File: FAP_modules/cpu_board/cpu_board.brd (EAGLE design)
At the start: 100 x 60 mm, 34 parts, among them IC2 74HC245DW, IC3 74HC245DW, IC4 74HC04D, IC7 74HC245DW, IC8 74HC245DW, IC9 74HC245DW

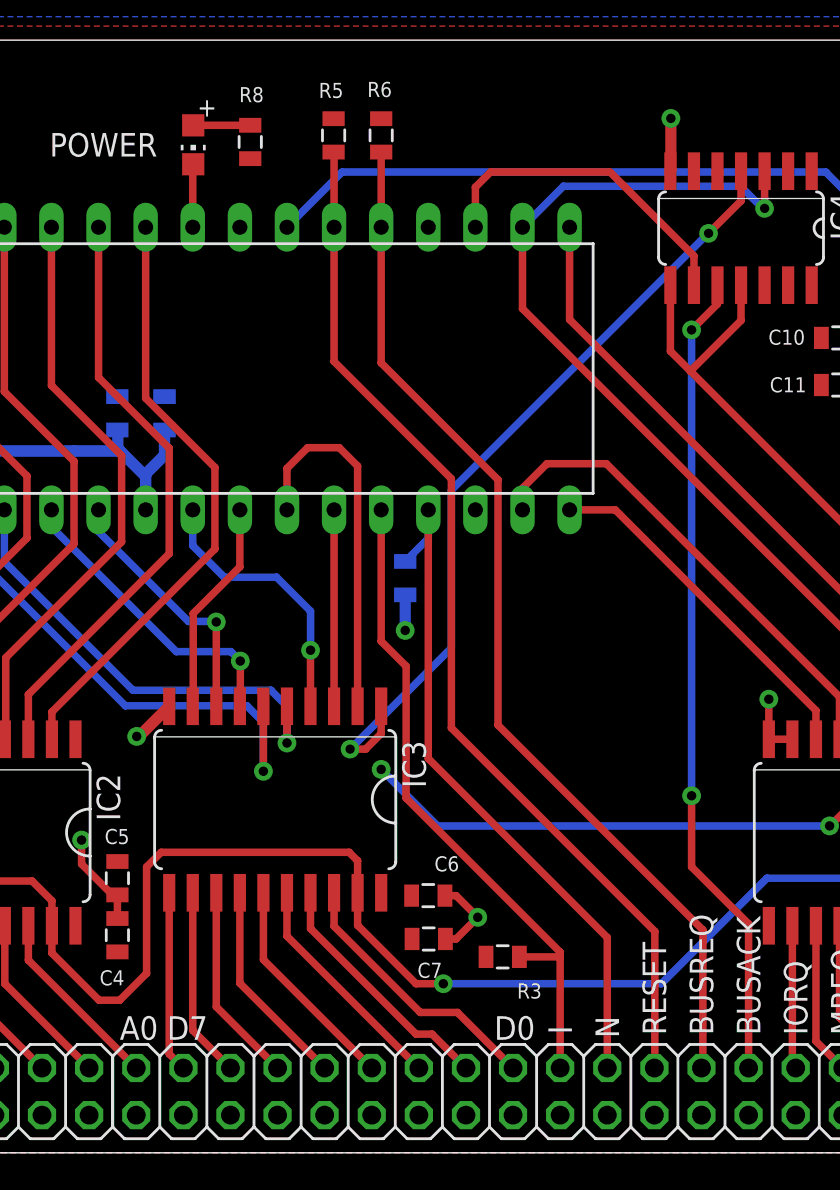
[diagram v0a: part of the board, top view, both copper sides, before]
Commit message: added interrupt chaining and WAIT
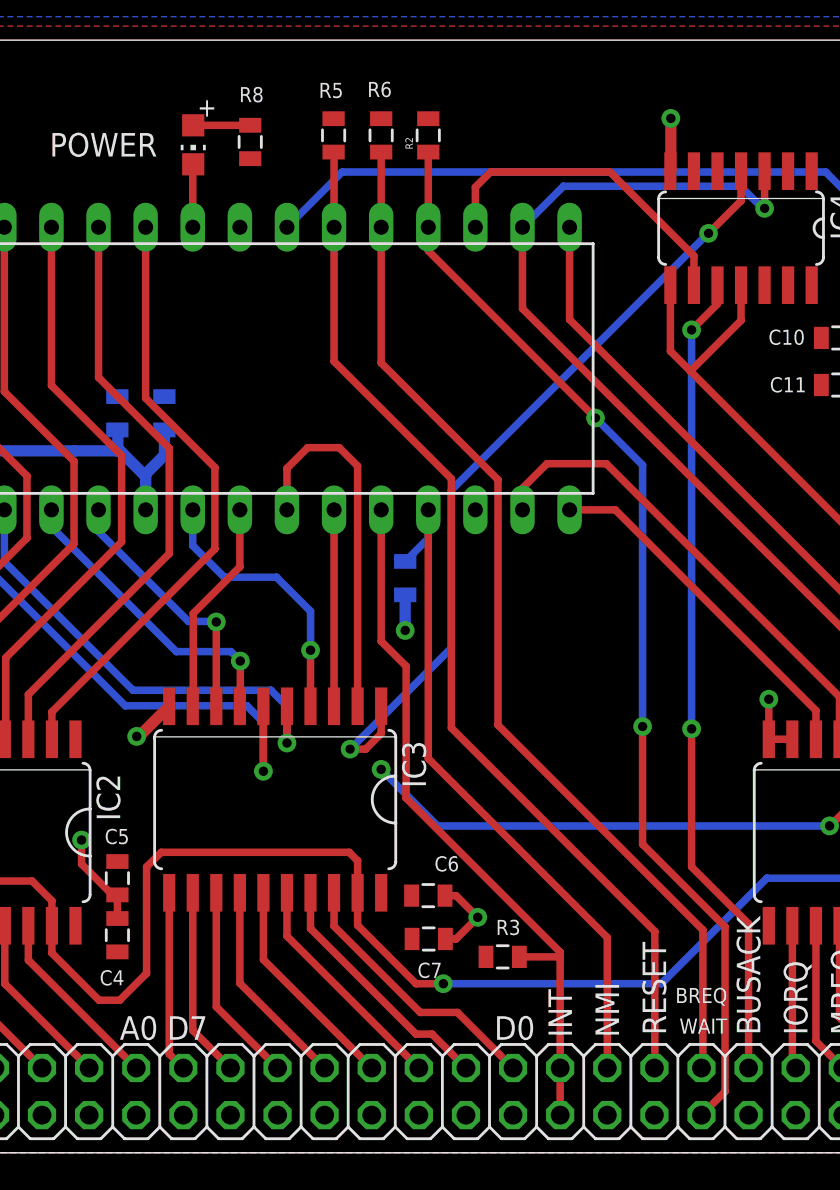
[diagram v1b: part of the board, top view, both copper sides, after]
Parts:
- added R2: (no value), SparkFun-Resistors:0805
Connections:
- new net N$32: IC1.24, R2.1, U$1.WAIT
- net +3V3: now also R2.2; no longer IC1.24
- net GND: no longer U$1.GND@29, U$1.GND@32
- net N$35: now also U$1.INTI, U$1.INTO; no longer U$1.INT
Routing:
- net N$32: track 0.00 -> 59.1 mm, vias 0 -> 2
- net N$35: track 36.3 -> 38.9 mm
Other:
- board text added: "BREQ"
- board text added: "INT"
- board text added: "NMI"
- board text added: "WAIT"
- board text removed: "BUSREQ"
- board text removed: "I"
- board text removed: "N"
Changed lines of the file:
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@@
 <?xml version="1.0" encoding="utf-8"?>
 <!DOCTYPE eagle SYSTEM "eagle.dtd">
-<eagle version="7.7.0">
+<eagle version="7.6.0">
 <drawing>
 <settings>
@@
 <setting verticaltext="up"/>
 </settings>
-<grid distance="20" unitdist="mil" unit="mil" style="lines" multiple="1" display="no" altdistance="0.5" altunitdist="mil" altunit="mil"/>
+<grid distance="5" unitdist="mil" unit="mil" style="lines" multiple="1" display="no" altdistance="0.5" altunitdist="mil" altunit="mil"/>
 <layers>
 <layer number="1" name="Top" color="4" fill="1" visible="yes" active="yes"/>
@@
 <text x="22.606" y="6.096" size="1.27" layer="25">A8</text>
 <text x="4.064" y="6.096" size="1.27" layer="25">A15</text>
-<text x="73.533" y="6.858" size="1.27" layer="25" rot="R270">I</text>
-<text x="76.073" y="7.366" size="1.27" layer="25" rot="R270">N</text>
+<text x="74.803" y="6.223" size="1.27" layer="25" rot="R90">INT</text>
+<text x="77.343" y="6.223" size="1.27" layer="25" rot="R90">NMI</text>
 <text x="79.883" y="6.35" size="1.27" layer="25" rot="R90">RESET</text>
-<text x="82.423" y="6.35" size="1.27" layer="25" rot="R90">BUSREQ</text>
+<text x="83.185" y="8.89" size="0.8128" layer="25" rot="R180">BREQ</text>
 <text x="84.963" y="6.35" size="1.27" layer="25" rot="R90">BUSACK</text>
 <text x="87.503" y="6.35" size="1.27" layer="25" rot="R90">IORQ</text>
@@
 dekuNukem 2016</text>
 <text x="46.6344" y="53.721" size="1.27" layer="25">POWER</text>
+<text x="83.185" y="7.239" size="0.8128" layer="25" rot="R180">WAIT</text>
 </plain>
 <attributes>
@@
 </element>
 <element name="R3" library="SparkFun-Resistors" package="0805" value="" x="71.0692" y="10.5664" smashed="yes" rot="R180">
-<attribute name="NAME" x="73.1774" y="9.1313" size="0.8128" layer="25" rot="R180"/>
+<attribute name="NAME" x="72.0344" y="12.5603" size="0.8128" layer="25" rot="R180"/>
 <attribute name="VALUE" x="72.0852" y="11.9634" size="0.4064" layer="27" rot="R180"/>
 </element>
@@
 </element>
 <element name="R1" library="SparkFun-Resistors" package="0805" value="" x="33.9598" y="15.875" rot="MR90"/>
+<element name="R2" library="SparkFun-Resistors" package="0805" value="" x="67.056" y="54.864" rot="R90"/>
 </elements>
 <signals>
@@
 <contactref element="R5" pad="2"/>
 <contactref element="R6" pad="2"/>
-<contactref element="IC1" pad="24"/>
 <contactref element="IC3" pad="20"/>
 <via x="65.8114" y="28.1686" extent="1-16" drill="0.508"/>
@@
 <wire x1="32.3723" y1="16.7767" x2="33.9581" y2="16.7767" width="0.4064" layer="16"/>
 <wire x1="33.9581" y1="16.7767" x2="33.9598" y2="16.775" width="0.4064" layer="16"/>
+<contactref element="R2" pad="2"/>
 </signal>
 <signal name="+5V">
@@
 <wire x1="82.6516" y1="45.7708" x2="81.2546" y2="44.3738" width="0.4064" layer="1"/>
 <via x="81.2546" y="44.3738" extent="1-16" drill="0.508"/>
-<via x="81.2546" y="19.2532" extent="1-16" drill="0.508"/>
-<wire x1="81.2546" y1="19.2532" x2="81.2546" y2="15.4178" width="0.4064" layer="1"/>
+<via x="81.2546" y="22.86" extent="1-16" drill="0.508"/>
+<wire x1="81.2546" y1="22.86" x2="81.2546" y2="15.4178" width="0.4064" layer="1"/>
 <wire x1="81.2546" y1="15.4178" x2="84.328" y2="12.3444" width="0.4064" layer="1"/>
-<wire x1="81.2546" y1="44.3738" x2="81.2546" y2="19.2532" width="0.4064" layer="16"/>
+<wire x1="81.2546" y1="44.3738" x2="81.2546" y2="22.86" width="0.4064" layer="16"/>
 </signal>
 <signal name="N$26">
@@
 <contactref element="IC1" pad="16"/>
 <contactref element="R3" pad="1"/>
-<contactref element="U$1" pad="INT"/>
+<contactref element="U$1" pad="INTI"/>
 <wire x1="64.516" y1="34.671" x2="64.516" y2="27.5844" width="0.4064" layer="1"/>
 <wire x1="64.516" y1="27.5844" x2="65.8622" y2="26.2382" width="0.4064" layer="1"/>
@@
 <wire x1="65.8622" y1="19.1262" x2="74.168" y2="10.8204" width="0.4064" layer="1"/>
 <wire x1="74.168" y1="10.8204" x2="74.168" y2="10.6172" width="0.4064" layer="1"/>
-<wire x1="74.168" y1="10.6172" x2="74.168" y2="4.572" width="0.4064" layer="1"/>
-<wire x1="71.9692" y1="10.5664" x2="74.1172" y2="10.5664" width="0.4064" layer="1"/>
+<wire x1="71.9692" y1="10.5664" x2="74.041" y2="10.5664" width="0.4064" layer="1"/>
+<wire x1="74.041" y1="10.5664" x2="74.1172" y2="10.5664" width="0.4064" layer="1"/>
 <wire x1="74.1172" y1="10.5664" x2="74.168" y2="10.6172" width="0.4064" layer="1"/>
+<contactref element="U$1" pad="INTO"/>
+<wire x1="74.168" y1="4.572" x2="74.168" y2="10.4394" width="0.4064" layer="1"/>
+<wire x1="74.168" y1="10.4394" x2="74.041" y2="10.5664" width="0.4064" layer="1"/>
+<wire x1="74.168" y1="4.572" x2="74.168" y2="2.032" width="0.4064" layer="1"/>
 </signal>
 <signal name="N$39">
@@
 <contactref element="U$1" pad="GND@21"/>
 <contactref element="U$1" pad="GND@7"/>
-<contactref element="U$1" pad="GND@29"/>
 <contactref element="U$1" pad="GND@23"/>
 <contactref element="U$1" pad="GND@30"/>
@@
 <contactref element="U$1" pad="GND@15"/>
 <contactref element="U$1" pad="GND@25"/>
-<contactref element="U$1" pad="GND@32"/>
 <contactref element="U$1" pad="GND@18"/>
 <contactref element="U$1" pad="GND@28"/>
@@
 <wire x1="83.9216" y1="51.3334" x2="83.9216" y2="52.9336" width="0.4064" layer="1"/>
 </signal>
+<signal name="N$32">
+<contactref element="U$1" pad="WAIT"/>
+<contactref element="IC1" pad="24"/>
+<contactref element="R2" pad="1"/>
+<wire x1="67.056" y1="53.964" x2="67.056" y2="49.911" width="0.4064" layer="1"/>
+<wire x1="67.056" y1="49.911" x2="67.056" y2="48.641" width="0.4064" layer="1"/>
+<wire x1="67.056" y1="48.641" x2="76.073" y2="39.624" width="0.4064" layer="1"/>
+<via x="76.073" y="39.624" extent="1-16" drill="0.5"/>
+<wire x1="76.073" y1="39.624" x2="78.613" y2="37.084" width="0.4064" layer="16"/>
+<wire x1="78.613" y1="37.084" x2="78.613" y2="22.987" width="0.4064" layer="16"/>
+<via x="78.613" y="22.987" extent="1-16" drill="0.5"/>
+<wire x1="78.613" y1="22.987" x2="78.613" y2="16.637" width="0.4064" layer="1"/>
+<wire x1="78.613" y1="16.637" x2="83.058" y2="12.192" width="0.4064" layer="1"/>
+<wire x1="83.058" y1="12.192" x2="83.058" y2="3.302" width="0.4064" layer="1"/>
+<wire x1="83.058" y1="3.302" x2="81.788" y2="2.032" width="0.4064" layer="1"/>
+</signal>
 </signals>

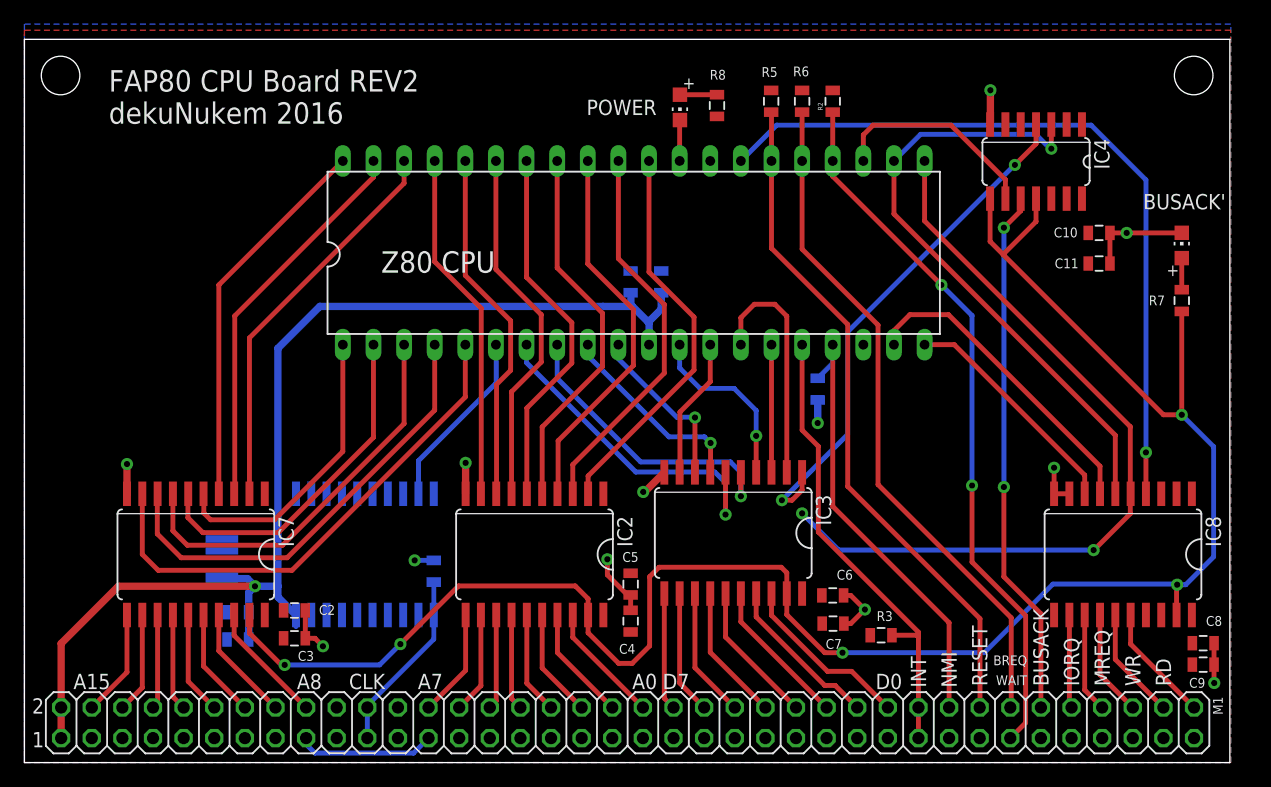
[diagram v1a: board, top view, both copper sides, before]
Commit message: new memory board
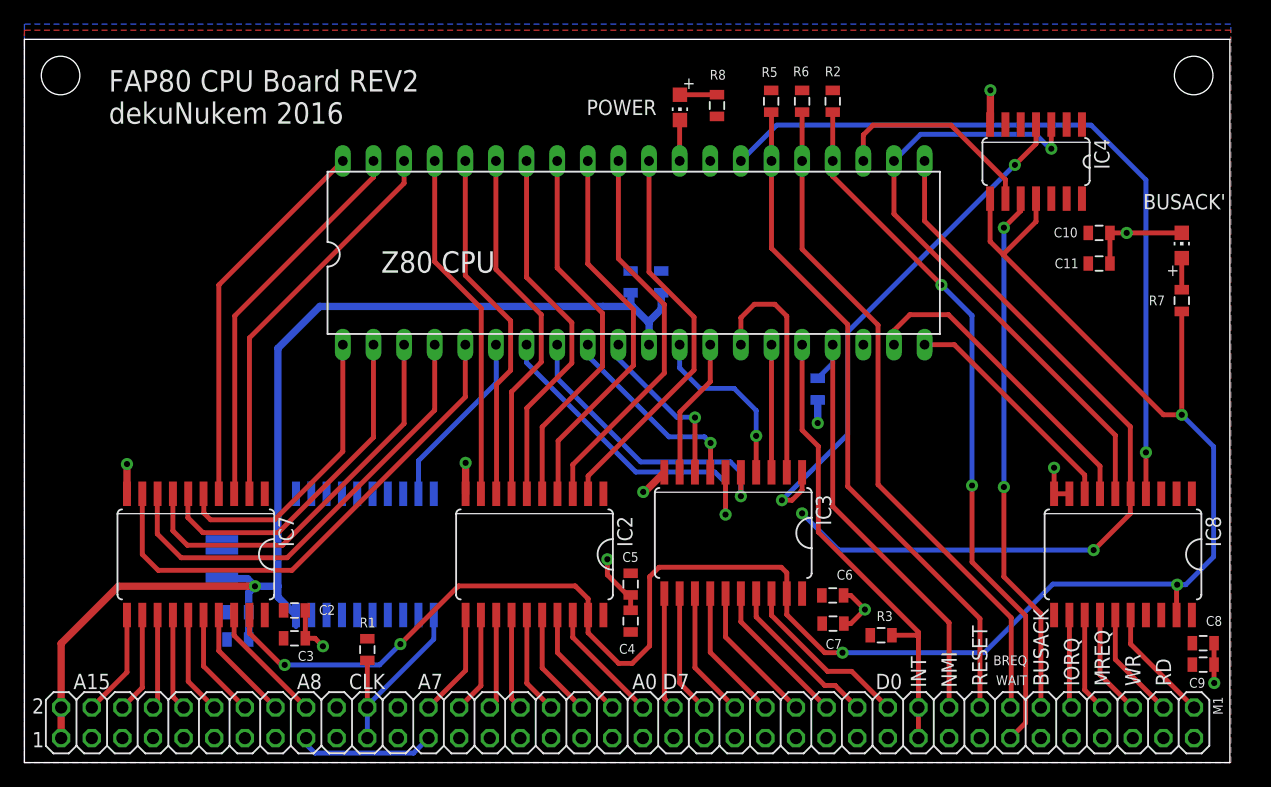
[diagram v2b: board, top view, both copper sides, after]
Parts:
- R1, R2, R3, R4, R5, R6: value (none) -> 4.7K
- R7, R8: value 50 -> 2K
- moved R1 8.52 mm to (28.4, 9.37), flipped to the top
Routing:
- net N$26: track 15.2 -> 16.9 mm
- net +3V3: track 3.51 -> 1.92 mm, vias 2 -> 1
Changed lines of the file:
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@@
 <?xml version="1.0" encoding="utf-8"?>
 <!DOCTYPE eagle SYSTEM "eagle.dtd">
-<eagle version="7.6.0">
+<eagle version="7.7.0">
 <drawing>
 <settings>
@@
 <setting verticaltext="up"/>
 </settings>
-<grid distance="5" unitdist="mil" unit="mil" style="lines" multiple="1" display="no" altdistance="0.5" altunitdist="mil" altunit="mil"/>
+<grid distance="1" unitdist="mil" unit="mil" style="lines" multiple="1" display="no" altdistance="0.5" altunitdist="mil" altunit="mil"/>
 <layers>
 <layer number="1" name="Top" color="4" fill="1" visible="yes" active="yes"/>
@@
 <attribute name="NAME" x="21.3868" y="20.447" size="1.27" layer="26" ratio="10" rot="MR270"/>
 </element>
-<element name="R3" library="SparkFun-Resistors" package="0805" value="" x="71.0692" y="10.5664" smashed="yes" rot="R180">
+<element name="R3" library="SparkFun-Resistors" package="0805" value="4.7K" x="71.0692" y="10.5664" smashed="yes" rot="R180">
 <attribute name="NAME" x="72.0344" y="12.5603" size="0.8128" layer="25" rot="R180"/>
 <attribute name="VALUE" x="72.0852" y="11.9634" size="0.4064" layer="27" rot="R180"/>
 </element>
-<element name="R4" library="SparkFun-Resistors" package="0805" value="" x="65.8114" y="30.988" smashed="yes" rot="MR270">
+<element name="R4" library="SparkFun-Resistors" package="0805" value="4.7K" x="65.8114" y="30.988" smashed="yes" rot="MR270">
 <attribute name="NAME" x="64.5795" y="31.5976" size="0.8128" layer="26" rot="MR270"/>
 <attribute name="VALUE" x="67.2084" y="32.004" size="0.4064" layer="28" rot="MR270"/>
 </element>
-<element name="R5" library="SparkFun-Resistors" package="0805" value="" x="61.9506" y="54.864" smashed="yes" rot="R90">
+<element name="R5" library="SparkFun-Resistors" package="0805" value="4.7K" x="61.9506" y="54.864" smashed="yes" rot="R90">
 <attribute name="NAME" x="62.484" y="57.6961" size="0.8128" layer="25" rot="R180"/>
-<attribute name="VALUE" x="63.3476" y="53.848" size="0.4064" layer="27" rot="R90"/>
-</element>
-<element name="R6" library="SparkFun-Resistors" package="0805" value="" x="64.516" y="54.864" smashed="yes" rot="R90">
+</element>
+<element name="R6" library="SparkFun-Resistors" package="0805" value="4.7K" x="64.516" y="54.864" smashed="yes" rot="R90">
 <attribute name="NAME" x="65.1002" y="57.7469" size="0.8128" layer="25" rot="R180"/>
-<attribute name="VALUE" x="65.913" y="53.848" size="0.4064" layer="27" rot="R90"/>
 </element>
 <element name="C2" library="SparkFun-Capacitors" package="0805" value="10nF" x="22.4028" y="12.6238" smashed="yes">
@@
 <attribute name="VALUE" x="98.552" y="41.6306" size="1.27" layer="27" rot="R90"/>
 </element>
-<element name="R7" library="SparkFun-Passives" package="0805" value="50" x="96.012" y="38.3286" smashed="yes" rot="R90">
+<element name="R7" library="SparkFun-Passives" package="0805" value="2K" x="96.012" y="38.3286" smashed="yes" rot="R90">
 <attribute name="NAME" x="94.615" y="38.7477" size="0.8128" layer="25" rot="R180"/>
 </element>
@@
 <attribute name="VALUE" x="51.8414" y="55.626" size="1.27" layer="27" rot="R270"/>
 </element>
-<element name="R8" library="SparkFun-Passives" package="0805" value="50" x="57.4548" y="54.5084" smashed="yes" rot="R90">
+<element name="R8" library="SparkFun-Passives" package="0805" value="2K" x="57.4548" y="54.5084" smashed="yes" rot="R90">
 <attribute name="NAME" x="58.1914" y="57.4675" size="0.8128" layer="25" rot="R180"/>
 </element>
-<element name="R1" library="SparkFun-Resistors" package="0805" value="" x="33.9598" y="15.875" rot="MR90"/>
-<element name="R2" library="SparkFun-Resistors" package="0805" value="" x="67.056" y="54.864" rot="R90"/>
+<element name="R1" library="SparkFun-Resistors" package="0805" value="4.7K" x="28.448" y="9.3726" smashed="yes" rot="R90">
+<attribute name="NAME" x="29.1338" y="12.0269" size="0.8128" layer="25" rot="R180"/>
+</element>
+<element name="R2" library="SparkFun-Resistors" package="0805" value="4.7K" x="67.056" y="54.864" smashed="yes" rot="R90">
+<attribute name="NAME" x="67.7418" y="57.7469" size="0.8128" layer="25" rot="R180"/>
+</element>
 </elements>
 <signals>
@@
 <contactref element="IC8" pad="3"/>
 <contactref element="R1" pad="2"/>
-<via x="32.3723" y="16.7767" extent="1-16" drill="0.508"/>
-<wire x1="32.3723" y1="16.7767" x2="33.9581" y2="16.7767" width="0.4064" layer="16"/>
-<wire x1="33.9581" y1="16.7767" x2="33.9598" y2="16.775" width="0.4064" layer="16"/>
 <contactref element="R2" pad="2"/>
 </signal>
@@
 <contactref element="U$1" pad="CLK"/>
 <contactref element="U$1" pad="CLK@2"/>
-<wire x1="28.448" y1="2.032" x2="28.448" y2="4.572" width="0.4064" layer="16"/>
 <contactref element="IC9" pad="11"/>
-<wire x1="28.448" y1="4.572" x2="28.448" y2="4.7244" width="0.4064" layer="16"/>
-<wire x1="28.448" y1="4.7244" x2="33.9598" y2="10.2362" width="0.4064" layer="16"/>
 <wire x1="33.9598" y1="10.2362" x2="33.9598" y2="12.2428" width="0.4064" layer="16"/>
 <contactref element="R1" pad="1"/>
-<wire x1="33.9598" y1="14.975" x2="33.9598" y2="12.2428" width="0.4064" layer="16"/>
+<wire x1="33.9598" y1="10.2362" x2="28.448" y2="4.7244" width="0.4064" layer="16"/>
+<wire x1="28.448" y1="4.7244" x2="28.448" y2="4.572" width="0.4064" layer="16"/>
+<wire x1="28.448" y1="4.572" x2="28.448" y2="4.064" width="0.4064" layer="16"/>
+<wire x1="28.448" y1="8.4726" x2="28.448" y2="4.572" width="0.4064" layer="1"/>
+<wire x1="28.448" y1="2.032" x2="28.448" y2="4.572" width="0.4064" layer="16"/>
 </signal>
 <signal name="N$27">

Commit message: board cleanup
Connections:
- net +3V3: now also IC4.1, IC4.13, IC4.5
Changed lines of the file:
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@@
 <contactref element="R1" pad="2"/>
 <contactref element="R2" pad="2"/>
+<contactref element="IC4" pad="1"/>
+<contactref element="IC4" pad="5"/>
+<contactref element="IC4" pad="13"/>
 </signal>
 <signal name="+5V">
